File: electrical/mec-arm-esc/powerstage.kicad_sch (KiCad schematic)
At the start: 12 parts, among them Q1 STL110N10F7, Q2 STL110N10F7, U1 L6387ED

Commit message: finish single phase
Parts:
- removed D1: D, symbol Device:D
- added C5: 10nF, symbol Device:C
- added D2: STPS0560Z, EasyEDA:SOD-123_L2.7-W1.6-LS3.7-RD, symbol core:STPS0560Z
- added R5: 1, symbol Device:R
- C1, C2: value C -> 100pF
- C3: value C -> 470nF
- C4: value C -> 1uF
- R1, R2: value R -> 10k
- R3, R4: value R -> 33
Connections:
- net +12V: now also D2.2
- net GND: now also C5.1
- net at C4.1, U1.8 (VBOOT): now also D2.1
- net PHASE A: now reaches C4.2
- net PHASE A: now also Q1.1 (S), Q1.2 (S), Q1.3 (S), Q2.5 (D), Q2.6 (D), Q2.7 (D), Q2.8 (D), Q2.9 (D), R1.1, U1.6 (OUT), R5.1
- net V_SHUNT_A+: now reaches Q2.1 (S)
- net V_SHUNT_A+: now also Q2.2 (S), Q2.3 (S), R2.2
- net at Q2.4 (G): now also R2.1, R4.2
- net at U1.5 (LVG): now also R4.1
- net at U1.7 (HVG): now also R3.1
- net at Q1.4 (G): now also R1.2, R3.2
- net VBUS: now reaches Q1.5 (D)
- net VBUS: now also Q1.6 (D), Q1.7 (D), Q1.8 (D), Q1.9 (D)
- new net: C5.2, R5.2
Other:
- moved on the sheet: C1, C2, C3, C4, Q1, Q2, R1, R2, R3, R4, U1

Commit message: added mcu sheet
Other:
- note added: "Current Sense Circuit sim for internal MCU Opamp"
- moved on the sheet: C1, C2, C3, C4, C5, D2, Q1, Q2, R1, R2, R3, R4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

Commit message: shunt phase a added
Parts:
- added C6: 220 pF, symbol Device:C
- added R6: SEWF3920D4L00P9, EasyEDA:RES-SMD_L10.0-W5.2-1, symbol core:SEWF3920D4L00P9
- added R7: 655, symbol Device:R
- added R8, R9: 22k, symbol Device:R
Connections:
- net GND: now also C6.2, R6.1, R8.2
- net V_SHUNT_A+: now also R6.2, R7.1
- new net +3V3: R9.1
- new net CURR_A_OP+: C6.1, R7.2, R8.1, R9.2

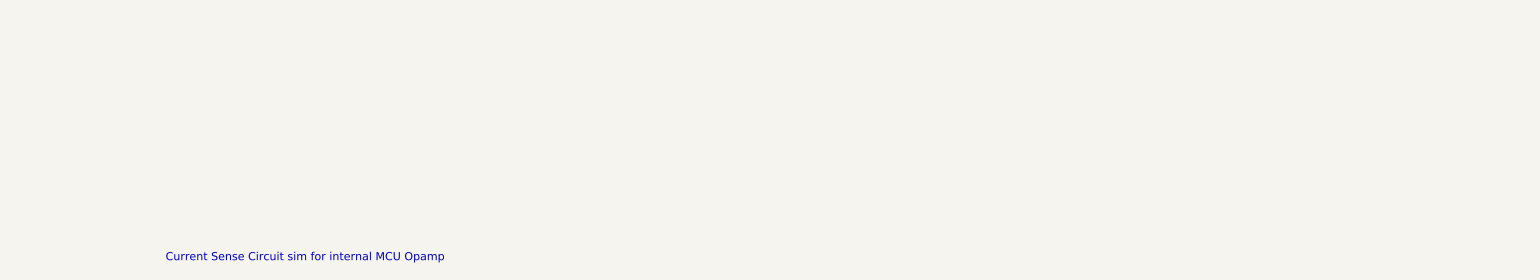
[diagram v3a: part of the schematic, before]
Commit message: added MCU power and ground + altered symbol
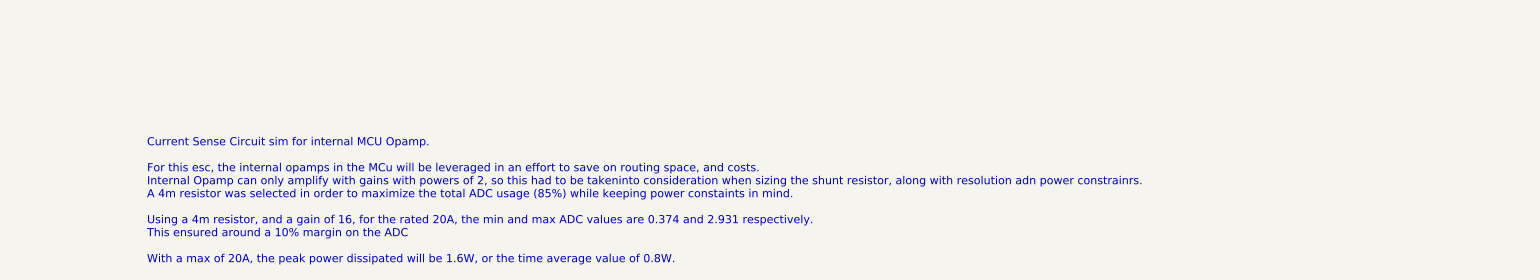
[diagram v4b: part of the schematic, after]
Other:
- note added: "Current Sense Circuit sim for internal MCU Opamp. For this esc, the internal opamps in the MCu will be leveraged in an effort to save on routing space, and costs. Internal Opamp can only amplify with gains with powers of 2, so this had to be takeninto consideration when sizing the shunt resistor, along with resolution adn power constrainrs. A 4m resistor was selected in order to maximize the tota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"
- note removed: "Current Sense Circuit sim for internal MCU Opamp"
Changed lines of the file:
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@@
 		(rev "V1")
 	)
-	(text "Current Sense Circuit sim for internal MCU Opamp\n"
+	(text "Current Sense Circuit sim for internal MCU Opamp.\n\nFor this esc, the internal opamps in the MCu will be leveraged in an effort to save on routing space, and costs. \nInternal Opamp can only amplify with gains with powers of 2, so this had to be takeninto consideration when sizing the shunt resistor, along with resolution adn power constrainrs. \nA 4m resistor was selected in order to maximize the total ADC usage (85%) while keeping power constaints in mind.\n\nUsing a 4m resistor, and a gain of 16, for the rated 20A, the min and max ADC values are 0.374 and 2.931 respectively.\nThis ensured around a 10% margin on the ADC\n\nWith a max of 20A, the peak power dissipated will be 1.6W, or the time average value of 0.8W.\n"
 		(exclude_from_sim no)
-		(at 446.278 122.428 0)
+		(at 421.386 113.538 0)
 		(effects
 			(font
 				(size 1.27 1.27)
 			)
+			(justify left)
 		)
 	)
@@
 	)
 	(image
-		(at 287.02 -81.28)
+		(at 520.7 205.74)
 		(scale 1.81946)
 		(data "iVBORw0KGgoAAAANSUhEUgAABQQAAAQqCAYAAAART3JpAAAABHNCSVQICAgIfAhkiAAAIABJREFU"
